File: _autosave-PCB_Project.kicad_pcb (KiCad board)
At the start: 8 copper layers, 60 x 70 mm, 203 parts, among them J1 Picoblade_CFG, J2 DF9-41P-1V32, J3 DF9-41P-1V32, U1 NX1H35 PBGA625, U10 TPS74201RGWR, U11 TPS3828-33DBVR, U12 MAX8556ETE, U13 TPS74201RGWR, U2 M95P32-IXMNT/E, U3 AS4C8M32S-6TIN, U4 AS4C8M16SA-6BIN, U5 CY15B108QN-40SXI, U6 CY15B108QN-40SXI, U7 CY15B108QN-40SXI, U8 MAX8556ETE, U9 MAX8556ETE, Y1 LFSPXO025225_25MHz

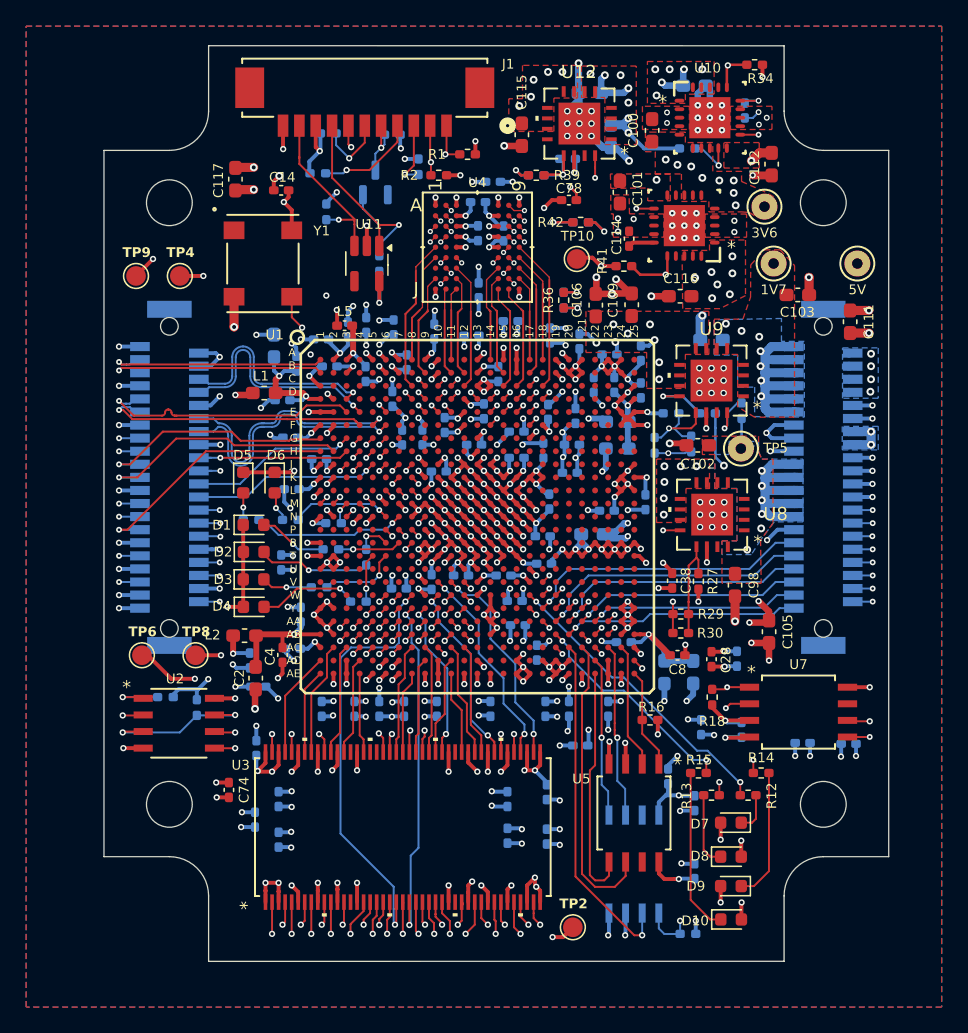
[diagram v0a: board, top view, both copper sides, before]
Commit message: pre-order adjustments
DF9 connectors footprint adjusted.
Dimensions of board edges changed.
Placement of DF9 adjusted.
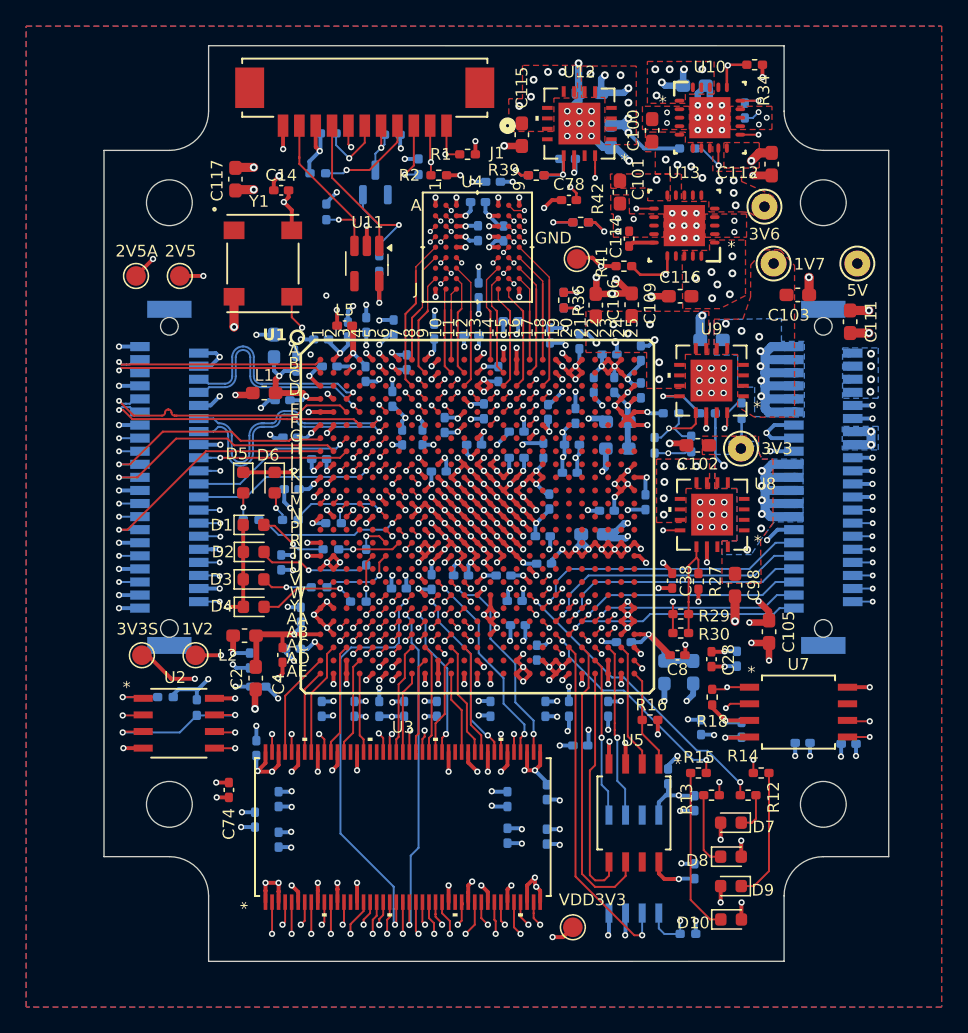
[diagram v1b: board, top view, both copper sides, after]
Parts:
- TP10: value TestPoint -> GND
- TP2: value TestPoint -> VDD3V3
- TP4: value TestPoint -> 2V5
- TP5: value TestPoint -> 3V3
- TP6: value TestPoint -> 3V3S
- TP8: value TestPoint -> 1V2
- TP9: value TestPoint -> 2V5A
